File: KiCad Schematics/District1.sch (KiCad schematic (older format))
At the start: 23 parts, among them M1 Fan, P2 TERM_08

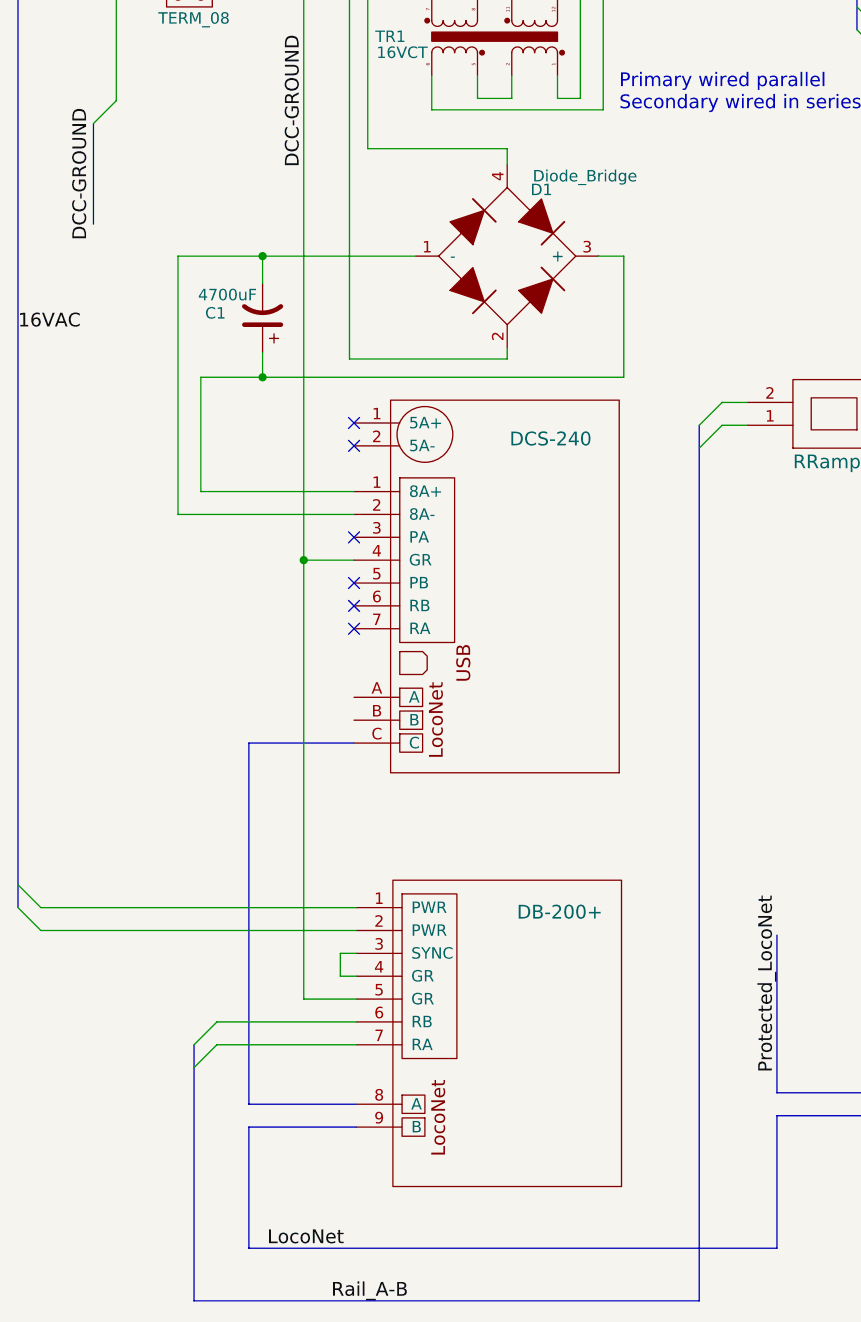
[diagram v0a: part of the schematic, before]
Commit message: Added R to power supply
Added a 1000 ohm bleeder resistor to the D1 power supply.
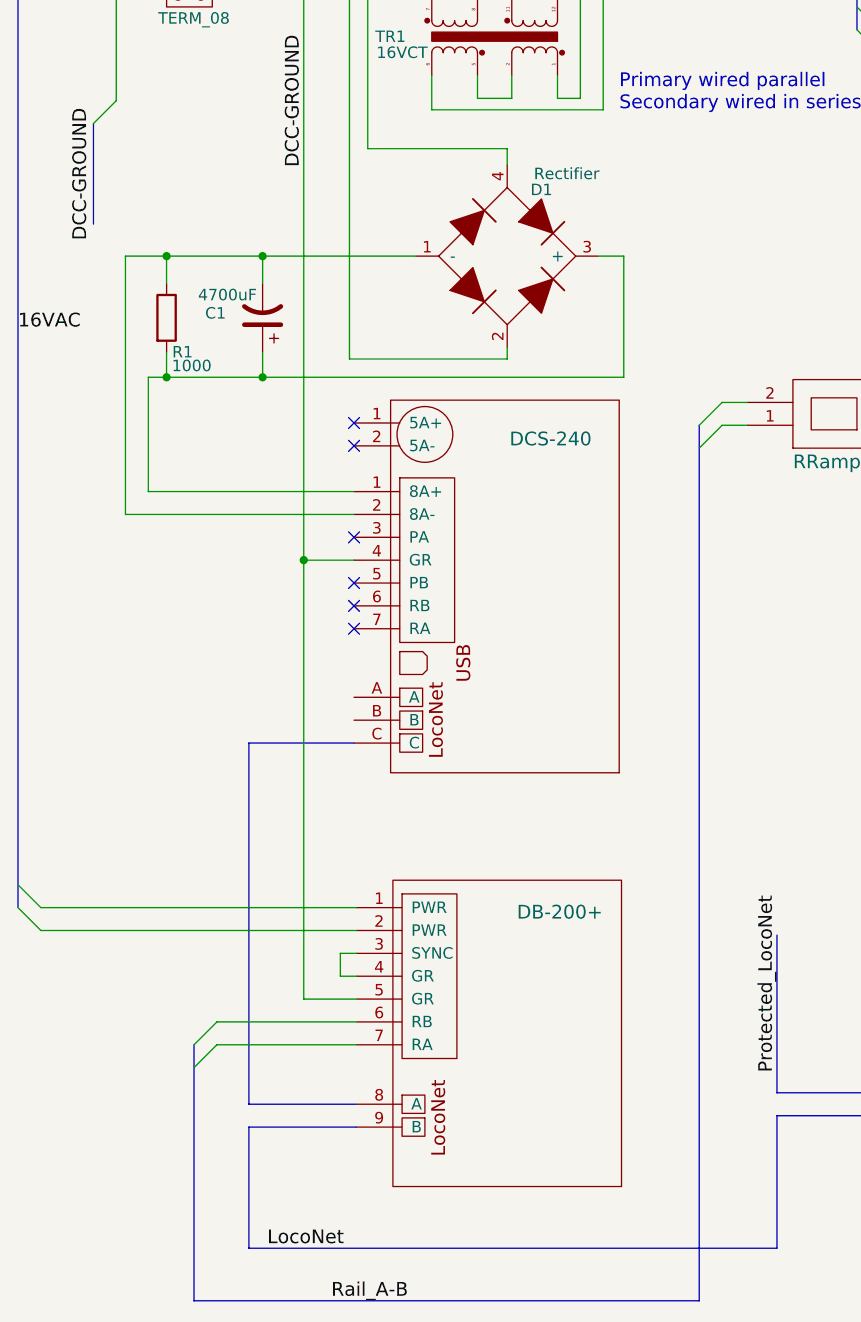
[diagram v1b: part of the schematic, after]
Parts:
- added R1: 1000, symbol R
- D1: value Diode_Bridge -> Rectifier
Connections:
- net at DCS1.1 (8A+): now also C1.1, D1.3 (+), R1.2
- net at DCS1.2 (8A-): now also C1.2, D1.1 (-), R1.1
- net at TB1.1 (P1): now also M1.1 (+)
- net at TB1.2 (P2): now also M1.2 (-)
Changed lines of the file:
@@
 P 2690 2790
 F 0 "D1" H 2840 3080 50  0000 C CNN
-F 1 "Diode_Bridge" H 3030 3140 50  0000 C CNN
+F 1 "Rectifier" H 2950 3150 50  0000 C CNN
 F 2 "" H 2690 2790 50  0000 C CNN
 F 3 "" H 2690 2790 50  0000 C CNN
@@
 Connection ~ 2000 1450
 Wire Wire Line
-	1250 2790 2290 2790
-Wire Wire Line
-	1250 2790 1250 3920
-Wire Wire Line
-	1250 3920 2020 3920
-Wire Wire Line
-	1350 3320 1350 3820
-Wire Wire Line
-	1350 3820 2020 3820
+	1020 2790 2290 2790
+Wire Wire Line
+	1020 2790 1020 3920
+Wire Wire Line
+	1020 3920 2020 3920
+Wire Wire Line
+	1120 3320 1120 3820
+Wire Wire Line
+	1120 3820 2020 3820
 Wire Wire Line
 	1050 1450 650  1450
@@
 	5160 3530 4520 3530
 Wire Bus Line
-	3530 7360 1320 7360
+	1320 7360 3530 7360
 Wire Wire Line
 	3740 3430 3630 3430
@@
 	3740 3530 3630 3530
 Wire Bus Line
-	3530 3530 3530 7360
+	3530 7360 3530 3530
 Wire Bus Line
 	3870 7130 3870 6550
@@
 	2080 2320 2080 1550
 Wire Wire Line
-	1350 3320 3200 3320
+	1120 3320 3200 3320
 Wire Wire Line
 	3200 3320 3200 2790
@@
 Text Notes 9890 860  2    60   ~ 0
 Wiring TBD
+$Comp
+L R R1
+U 1 1 57C2E4CC
+P 1200 3060
+F 0 "R1" H 1270 2910 50  0000 C CNN
+F 1 "1000" H 1310 2850 50  0000 C CNN
+F 2 "" V 1130 3060 50  0000 C CNN
+F 3 "" H 1200 3060 50  0000 C CNN
+	1    1200 3060
+	1    0    0    -1
+$EndComp
+Wire Wire Line
+	1200 2910 1200 2790
+Connection ~ 1200 2790
+Wire Wire Line
+	1200 3210 1200 3320
+Connection ~ 1200 3320
 $EndSCHEMATC
